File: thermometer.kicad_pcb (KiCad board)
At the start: 2 copper layers, 58 x 36.7 mm, 21 parts, among them IC1 ATTINY2313A-P, P1 CONN_4, P2 CONN_4, P3 CONN_6, P4 CONN_4

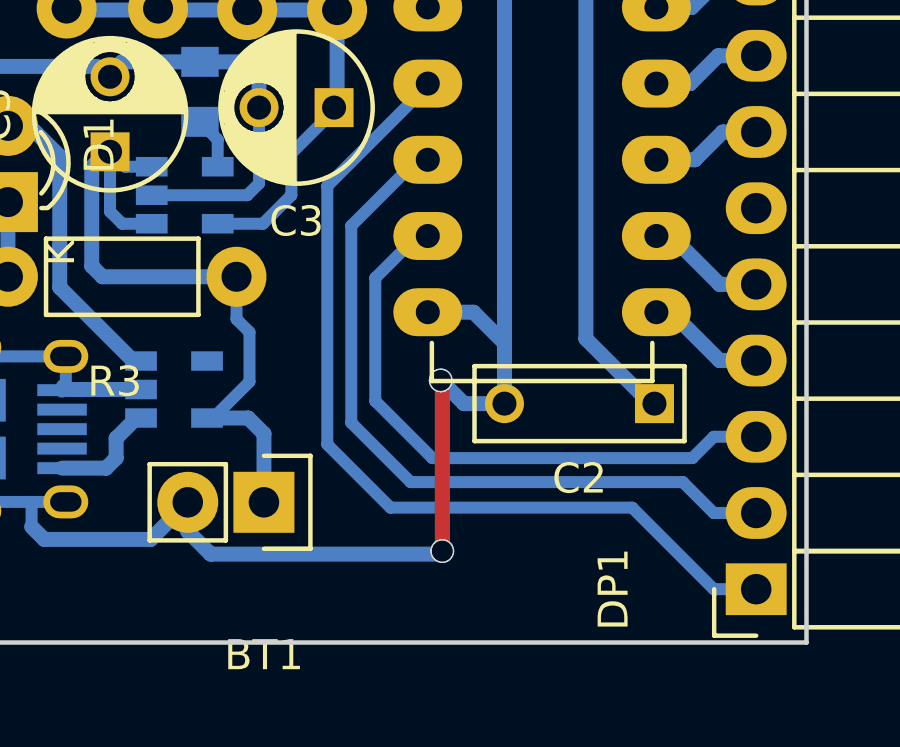
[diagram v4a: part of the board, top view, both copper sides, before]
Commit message: Fix Display
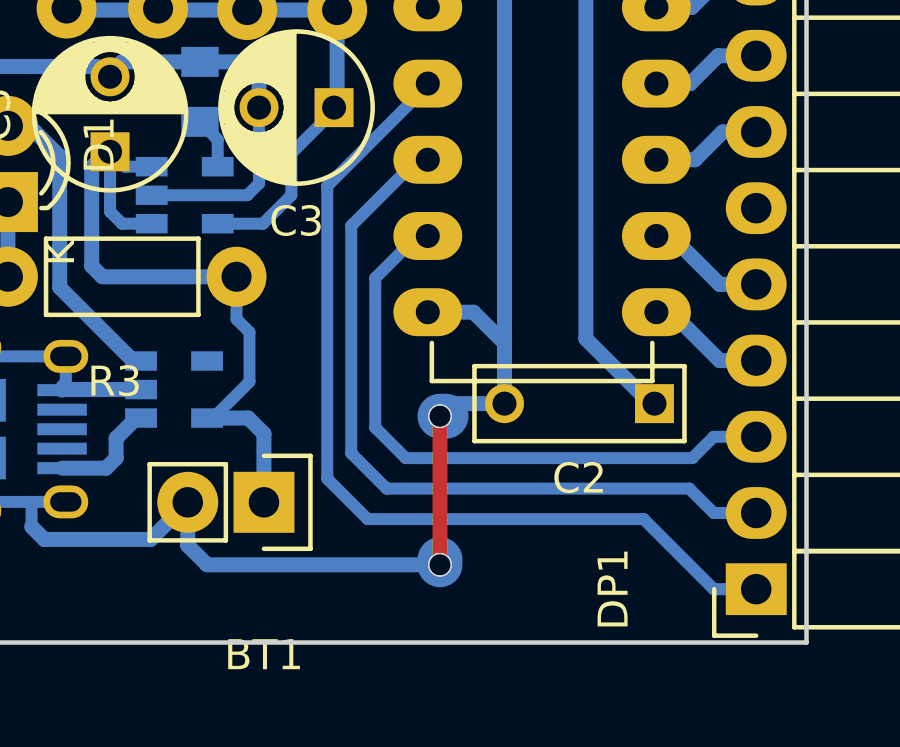
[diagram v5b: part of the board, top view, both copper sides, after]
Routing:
- net Net-(DP1-Pad1): track 30.4 -> 31.0 mm
- net Net-(DP1-Pad2): track 25.1 -> 25.7 mm
- net Net-(DP1-Pad3): track 21.0 -> 21.5 mm
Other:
- net class Default: trace_width 0.4 -> 1.5
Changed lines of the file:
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@@
   (general
     (links 66)
-    (no_connects 4)
+    (no_connects 3)
     (area 122.098999 79.884199 180.211801 116.711801)
     (thickness 1.6)
     (drawings 10)
-    (tracks 243)
+    (tracks 244)
     (zones 0)
     (modules 21)
@@
   )
   (setup
-    (last_trace_width 0.4)
+    (last_trace_width 1.5)
     (trace_clearance 0.4)
     (zone_clearance 0.508)
@@
   (net_class Default "Это класс цепей по умолчанию."
     (clearance 0.4)
-    (trace_width 0.4)
+    (trace_width 1.5)
     (via_dia 0.8)
     (via_drill 0.7)
@@
   (segment (start 133.1824 109.154) (end 131.8084 109.154) (width 0.5) (layer B.Cu) (net 6) (status 20))
   (segment (start 131.8084 109.154) (end 131.8236 109.1692) (width 0.5) (layer B.Cu) (net 6) (status 30))
+  (segment (start 139.573 113.87201) (end 139.573 114.046) (width 1.5) (layer B.Cu) (net 7))
+  (segment (start 139.573 109.092994) (end 139.772994 109.092994) (width 1.5) (layer B.Cu) (net 7))
+  (segment (start 139.573 109.092994) (end 139.992094 108.6739) (width 0.4) (layer B.Cu) (net 7))
+  (segment (start 141.7231 108.6739) (end 139.992094 108.6739) (width 0.5) (layer B.Cu) (net 7))
+  (via (at 139.573 109.092994) (size 0.8) (drill 0.7) (layers F.Cu B.Cu) (net 7))
+  (segment (start 139.573 114.046) (end 139.573 109.092994) (width 0.5) (layer F.Cu) (net 7))
+  (segment (start 139.007315 114.046) (end 139.573 114.046) (width 0.5) (layer B.Cu) (net 7))
+  (segment (start 131.81156 114.046) (end 139.007315 114.046) (width 0.5) (layer B.Cu) (net 7))
+  (segment (start 131.1656 111.9632) (end 131.1656 113.40004) (width 0.5) (layer B.Cu) (net 7))
+  (segment (start 131.1656 113.40004) (end 131.81156 114.046) (width 0.5) (layer B.Cu) (net 7))
+  (via (at 139.573 114.046) (size 0.8) (drill 0.7) (layers F.Cu B.Cu) (net 7))
   (segment (start 127.101 107.0998) (end 127.101 108.0498) (width 0.4) (layer B.Cu) (net 7))
   (segment (start 127.101 108.0498) (end 127.076001 108.074799) (width 0.4) (layer B.Cu) (net 7))
@@
   (segment (start 124.46 97.4344) (end 124.46 97.6884) (width 0.5) (layer B.Cu) (net 7))
   (segment (start 124.1044 96.8756) (end 124.46 97.2312) (width 0.5) (layer B.Cu) (net 7))
-  (segment (start 141.7231 108.6739) (end 140.3731 108.6739) (width 0.5) (layer B.Cu) (net 7) (status 10))
-  (segment (start 131.9276 113.6904) (end 131.1656 112.9284) (width 0.5) (layer B.Cu) (net 7) (status 20))
-  (segment (start 139.5476 113.6904) (end 131.9276 113.6904) (width 0.5) (layer B.Cu) (net 7))
-  (segment (start 139.6492 113.5888) (end 139.5476 113.6904) (width 0.5) (layer B.Cu) (net 7))
-  (via (at 139.6492 113.5888) (size 0.8) (drill 0.7) (layers F.Cu B.Cu) (net 7))
-  (segment (start 139.6492 107.95) (end 139.6492 113.5888) (width 0.5) (layer F.Cu) (net 7))
-  (segment (start 139.5984 107.8992) (end 139.6492 107.95) (width 0.5) (layer F.Cu) (net 7))
-  (via (at 139.5984 107.8992) (size 0.8) (drill 0.7) (layers F.Cu B.Cu) (net 7))
-  (segment (start 140.3731 108.6739) (end 139.5984 107.8992) (width 0.5) (layer B.Cu) (net 7))
-  (segment (start 131.1656 112.9284) (end 131.1656 111.9632) (width 0.5) (layer B.Cu) (net 7) (status 30))
   (segment (start 135.636 83.9216) (end 135.636 83.7184) (width 0.5) (layer B.Cu) (net 7) (status 30))
   (segment (start 135.636 83.7184) (end 138.1252 81.2292) (width 0.5) (layer B.Cu) (net 7) (status 10))
@@
   (segment (start 140.6906 105.6259) (end 141.7231 106.6584) (width 0.5) (layer B.Cu) (net 7))
   (segment (start 150.114 114.8588) (end 148.698 114.8588) (width 0.4) (layer B.Cu) (net 8))
-  (segment (start 148.698 114.8588) (end 145.9802 112.141) (width 0.4) (layer B.Cu) (net 8))
-  (segment (start 145.9802 112.141) (end 137.922 112.141) (width 0.4) (layer B.Cu) (net 8))
-  (segment (start 135.81657 110.03557) (end 135.81657 101.41943) (width 0.4) (layer B.Cu) (net 8))
-  (segment (start 137.922 112.141) (end 135.81657 110.03557) (width 0.4) (layer B.Cu) (net 8))
+  (segment (start 148.698 114.8588) (end 146.3612 112.522) (width 0.4) (layer B.Cu) (net 8))
+  (segment (start 146.3612 112.522) (end 137.16 112.522) (width 0.4) (layer B.Cu) (net 8))
+  (segment (start 139.1666 98.0694) (end 139.1666 98.0059) (width 0.4) (layer B.Cu) (net 8))
+  (segment (start 137.16 112.522) (end 135.81657 111.17857) (width 0.4) (layer B.Cu) (net 8))
+  (segment (start 135.81657 111.17857) (end 135.81657 101.41943) (width 0.4) (layer B.Cu) (net 8))
   (segment (start 135.81657 101.41943) (end 139.1666 98.0694) (width 0.4) (layer B.Cu) (net 8))
-  (segment (start 139.1666 98.0694) (end 139.1666 98.0059) (width 0.4) (layer B.Cu) (net 8))
   (segment (start 138.8166 98.0059) (end 139.1666 98.0059) (width 0.4) (layer B.Cu) (net 8))
   (segment (start 150.114 114.8588) (end 149.9616 114.8588) (width 0.4) (layer B.Cu) (net 8))
   (segment (start 139.1666 98.0059) (end 139.0269 98.0059) (width 0.5) (layer B.Cu) (net 8) (status 30))
-  (segment (start 138.59501 111.29001) (end 136.61658 109.31158) (width 0.4) (layer B.Cu) (net 9))
-  (segment (start 136.61658 109.31158) (end 136.61658 102.74592) (width 0.4) (layer B.Cu) (net 9))
+  (segment (start 150.114 112.3188) (end 148.698 112.3188) (width 0.4) (layer B.Cu) (net 9))
+  (segment (start 147.8852 111.506) (end 137.795 111.506) (width 0.4) (layer B.Cu) (net 9))
+  (segment (start 148.698 112.3188) (end 147.8852 111.506) (width 0.4) (layer B.Cu) (net 9))
+  (segment (start 137.795 111.506) (end 136.61658 110.32758) (width 0.4) (layer B.Cu) (net 9))
+  (segment (start 136.61658 110.32758) (end 136.61658 102.74592) (width 0.4) (layer B.Cu) (net 9))
   (segment (start 136.61658 102.74592) (end 138.8166 100.5459) (width 0.4) (layer B.Cu) (net 9))
   (segment (start 138.8166 100.5459) (end 139.1666 100.5459) (width 0.4) (layer B.Cu) (net 9))
-  (segment (start 147.66921 111.29001) (end 138.59501 111.29001) (width 0.4) (layer B.Cu) (net 9))
-  (segment (start 150.114 112.3188) (end 148.698 112.3188) (width 0.4) (layer B.Cu) (net 9))
-  (segment (start 148.698 112.3188) (end 147.66921 111.29001) (width 0.4) (layer B.Cu) (net 9))
   (segment (start 139.1666 100.5459) (end 138.8745 100.5459) (width 0.5) (layer B.Cu) (net 9) (status 30))
-  (segment (start 139.319 110.49) (end 137.41659 108.58759) (width 0.4) (layer B.Cu) (net 10))
-  (segment (start 137.41659 108.58759) (end 137.41659 104.48591) (width 0.4) (layer B.Cu) (net 10))
+  (segment (start 150.114 109.7788) (end 148.698 109.7788) (width 0.4) (layer B.Cu) (net 10))
+  (segment (start 148.698 109.7788) (end 147.9868 110.49) (width 0.4) (layer B.Cu) (net 10))
+  (segment (start 147.9868 110.49) (end 138.43 110.49) (width 0.4) (layer B.Cu) (net 10))
+  (segment (start 137.41659 109.47659) (end 137.41659 104.48591) (width 0.4) (layer B.Cu) (net 10))
+  (segment (start 138.43 110.49) (end 137.41659 109.47659) (width 0.4) (layer B.Cu) (net 10))
   (segment (start 137.41659 104.48591) (end 138.8166 103.0859) (width 0.4) (layer B.Cu) (net 10))
   (segment (start 138.8166 103.0859) (end 139.1666 103.0859) (width 0.4) (layer B.Cu) (net 10))
-  (segment (start 147.9868 110.49) (end 139.319 110.49) (width 0.4) (layer B.Cu) (net 10))
-  (segment (start 150.114 109.7788) (end 148.698 109.7788) (width 0.4) (layer B.Cu) (net 10))
-  (segment (start 148.698 109.7788) (end 147.9868 110.49) (width 0.4) (layer B.Cu) (net 10))
   (segment (start 139.1666 103.0859) (end 139.100602 103.0859) (width 0.5) (layer B.Cu) (net 10) (status 30))
   (segment (start 149.9616 110.1979) (end 150.4696 109.6899) (width 0.5) (layer B.Cu) (net 10) (status 30))

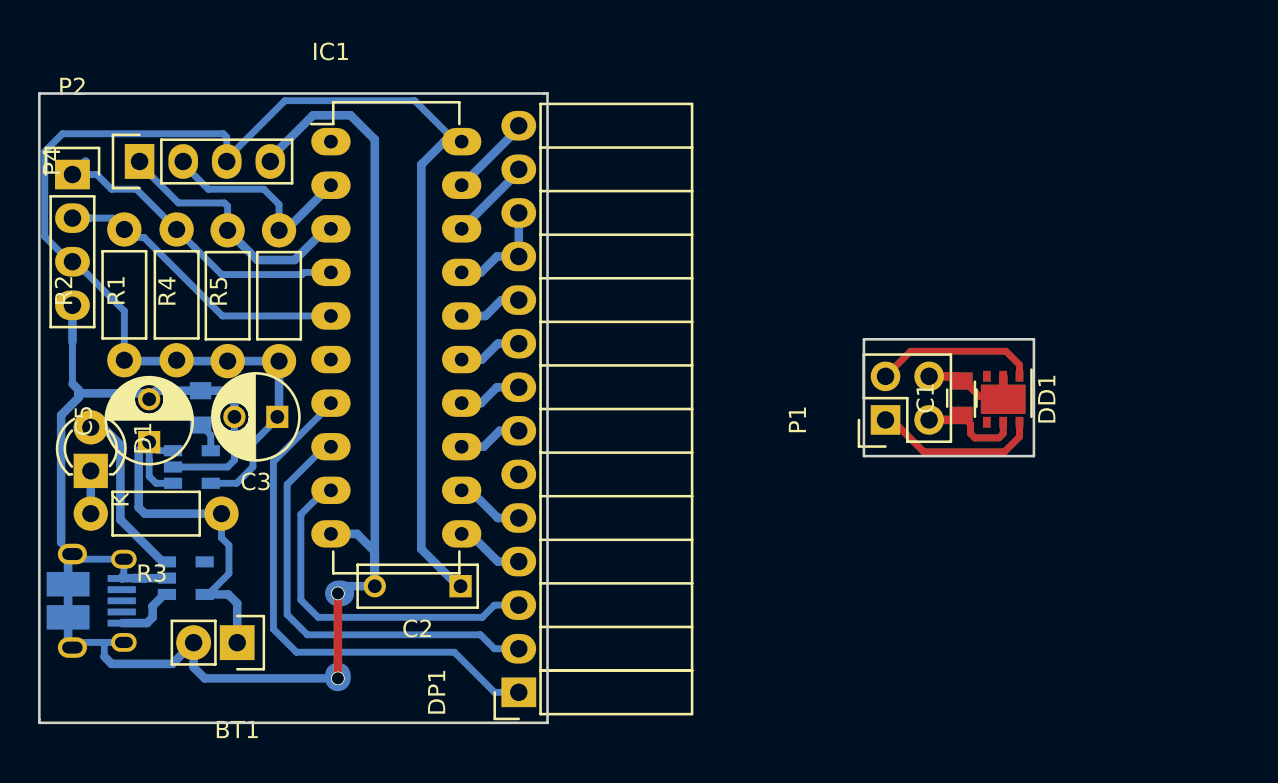
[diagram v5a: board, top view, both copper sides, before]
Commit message: Add power supply for temperature sensor.
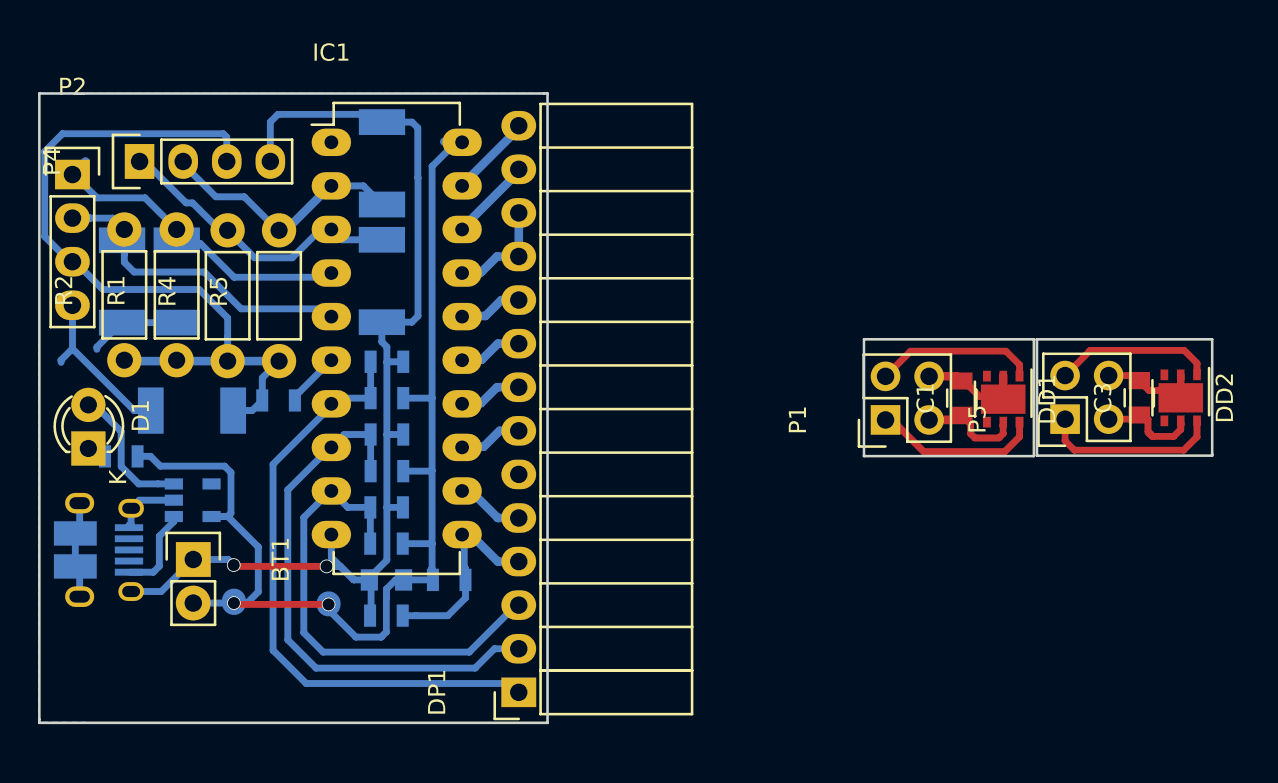
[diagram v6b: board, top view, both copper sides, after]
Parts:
- removed C4: 0.1, Capacitors_SMD:C_0805
- removed C5: 1.0, Capacitors_ThroughHole:C_Radial_D5_L6_P2.5
- removed DA1: LDK120, TO_SOT_Packages_SMD:SOT-23-5
- added D3: 3.3v, Diodes_SMD:MELF_Standard, B.Cu at (130.2, 90.9)
- added D4: 3.3v, Diodes_SMD:MELF_Standard, B.Cu at (127.0, 90.9)
- added D5: 3.3v, Diodes_SMD:MELF_Standard, B.Cu at (131.1, 98.4)
- added D6: 3.3v, Diodes_SMD:MELF_Standard, B.Cu at (142.1, 90.9)
- added D7: 3.3v, Diodes_SMD:MELF_Standard, B.Cu at (142.1, 84.0)
- added DD2: Si705x, Housings_DFN_QFN:DFN-6-1EP_3x3mm_Pitch0.95mm, F.Cu at (188.7, 97.7)
- added P5: CONN_4, Pin_Headers:Pin_Header_Straight_2x02, F.Cu at (182.0, 98.9)
- added R10: 1M, Resistors_SMD:R_0805, B.Cu at (142.4, 106.2)
- added R11: 1M, Resistors_SMD:R_0805, B.Cu at (142.4, 104.1)
- added R12: 1M, Resistors_SMD:R_0805, B.Cu at (146.1, 108.3)
- added R13: 1M, Resistors_SMD:R_0805, B.Cu at (142.4, 110.4)
- added R14: 100, Resistors_SMD:R_0805, B.Cu at (136.1, 97.8)
- added R6: 1M, Resistors_SMD:R_0805, B.Cu at (142.4, 97.7)
- added R7: 1M, Resistors_SMD:R_0805, B.Cu at (142.4, 95.6)
- added R8: 1M, Resistors_SMD:R_0805, B.Cu at (142.4, 102.0)
- added R9: 1M, Resistors_SMD:R_0805, B.Cu at (142.4, 99.8)
- C2: footprint Capacitors_ThroughHole:C_Rect_L7_W2.5_P5 -> Capacitors_SMD:C_0805; moved to B.Cu
- C3: value 1.0 -> 0.1; footprint Capacitors_ThroughHole:C_Radial_D5_L6_P2.5 -> Capacitors_SMD:C_0805
- R3: footprint Resistors_ThroughHole:Resistor_Horizontal_RM7mm -> Resistors_SMD:R_0805; moved to B.Cu
- moved C3 50.2 mm to (186.3, 97.7), turned to 90 degrees
- moved R3 6.73 mm to (126.9, 101.1)
- moved BT1 5.48 mm to (131.1, 107.1), turned to 270 degrees
- moved D2 4.56 mm to (131.1, 103.7)
- moved C2 4.34 mm to (142.4, 108.3)
- moved P3 3.00 mm to (125.9, 106.6)
- moved D1 1.32 mm to (125.0, 100.6)
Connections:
- BT1 pad 1: Net-(BT1-Pad1) -> GNDPWR
- BT1 pad 2: GNDPWR -> VDD
- C3 pad 1: VDD -> VCC
- C3 pad 2: GNDPWR -> GND
- D2 pad 4: (no net) -> Net-(D2-Pad4)
- D2 pad 5: Net-(BT1-Pad1) -> VDD
- DP1 pad 6: (no net) -> Net-(DP1-Pad6)
- IC1 pad 1: (no net) -> Net-(IC1-Pad1)
- IC1 pad 6: (no net) -> Net-(IC1-Pad6)
- P2 pad 3: VDD -> Net-(D5-Pad2)
- P3 pad 2: (no net) -> Net-(P3-Pad2)
- P3 pad 3: (no net) -> Net-(P3-Pad3)
- P3 pad 4: (no net) -> Net-(P3-Pad4)
- P4 pad 3: VDD -> Net-(D5-Pad2)
- R1 pad 1: VDD -> Net-(D5-Pad2)
- R2 pad 1: VDD -> Net-(D5-Pad2)
- R3 pad 1: Net-(BT1-Pad1) -> VDD
- R4 pad 1: VDD -> Net-(D5-Pad2)
- R5 pad 1: VDD -> Net-(D5-Pad2)
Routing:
- net Net-(D5-Pad2): track 0.00 -> 46.7 mm
- net Net-(BT1-Pad1): track 24.2 -> 0.00 mm
- net VDD: track 90.1 -> 67.7 mm, vias 0 -> 2
- net GNDPWR: track 111.2 -> 89.2 mm
- net Net-(DD2-Pad6): track 0.00 -> 10.3 mm
- net Net-(DD2-Pad1): track 0.00 -> 9.17 mm
- net GND: track 7.36 -> 16.4 mm
- net Net-(DP1-Pad4): track 4.00 -> 11.8 mm
- net Net-(DP1-Pad3): track 21.5 -> 28.7 mm
- net Net-(DP1-Pad2): track 25.7 -> 31.9 mm
- net VCC: track 6.12 -> 12.0 mm
- net Net-(DP1-Pad1): track 31.0 -> 36.5 mm
- net Net-(IC1-Pad6): track 0.00 -> 3.23 mm
- net Net-(D6-Pad2): track 15.2 -> 18.3 mm
- net Net-(D1-Pad2): track 11.0 -> 8.09 mm
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- added copper zone on B.Cu, net GNDPWR
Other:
- board size 58 x 36.7 mm -> 68.4 x 36.7 mm
- net class Default: trace_width 1.5 -> 0.4
